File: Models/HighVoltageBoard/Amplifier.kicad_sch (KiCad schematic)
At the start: 13 parts, among them J4 Conn_01x03_Socket, J8 Conn_Coaxial, Q1 Q_NJFET_DSG, Q5 Q_NJFET_DSG, U1 PA95

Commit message: Save progress
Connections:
- net -IN: now also NT1.1; no longer NT1.2
- net SENSEN: now also NT1.2; no longer NT1.1
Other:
- moved on the sheet: NT1, R1, R5

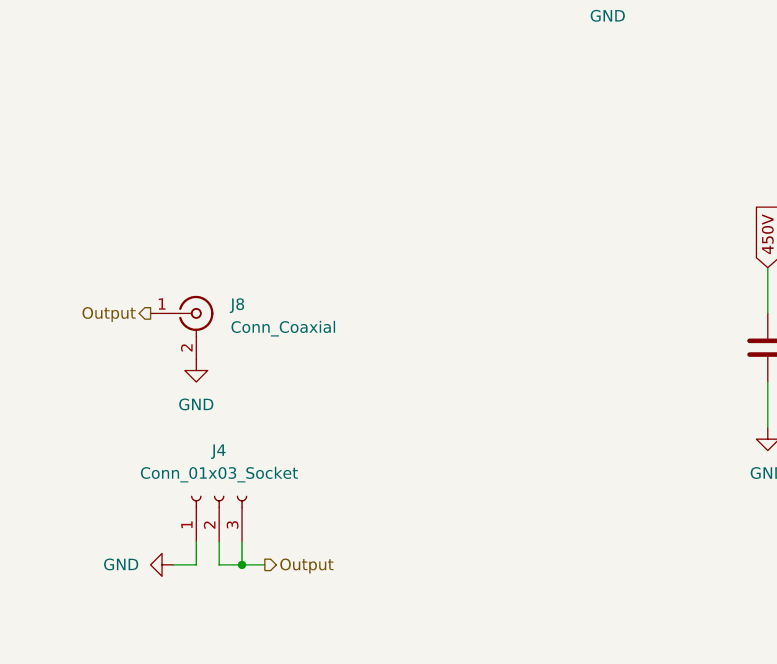
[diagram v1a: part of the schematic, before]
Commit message: Connectors should be fully specified now
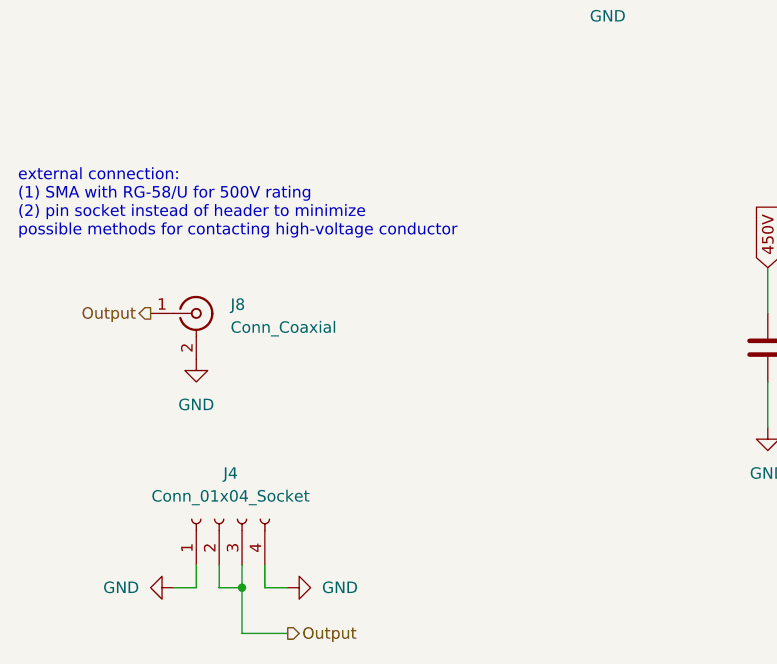
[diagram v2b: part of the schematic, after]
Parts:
- removed J4: Conn_01x03_Socket, symbol Connector:Conn_01x03_Socket
- added J4: Conn_01x04_Socket, symbol Connector:Conn_01x04_Socket
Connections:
- net GND: now also J4.1 (Pin_1), J4.4 (Pin_4)
- net Output: now also J4.2 (Pin_2), J4.3 (Pin_3)
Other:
- note added: "external connection: (1) SMA with RG-58/U for 500V rating (2) pin socket instead of header to minimize possible methods for contacting high-voltage conductor"

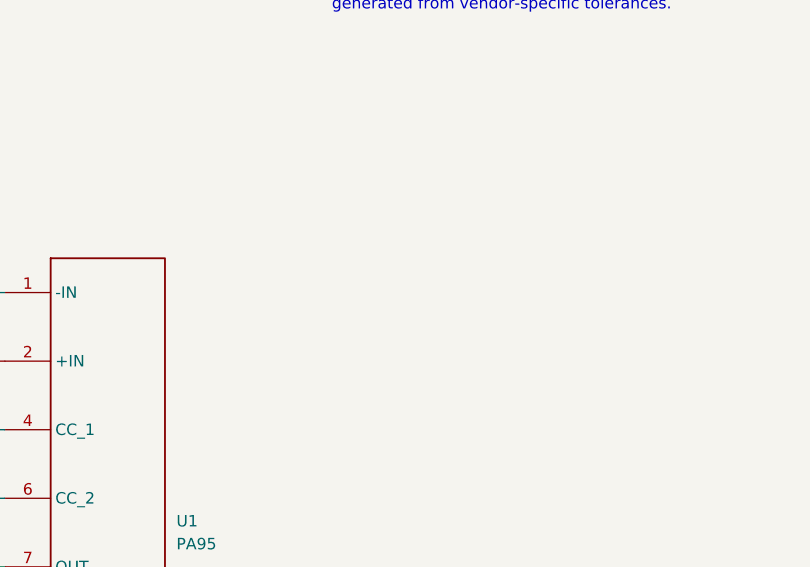
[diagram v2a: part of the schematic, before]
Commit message: Updated exclude from BOMs
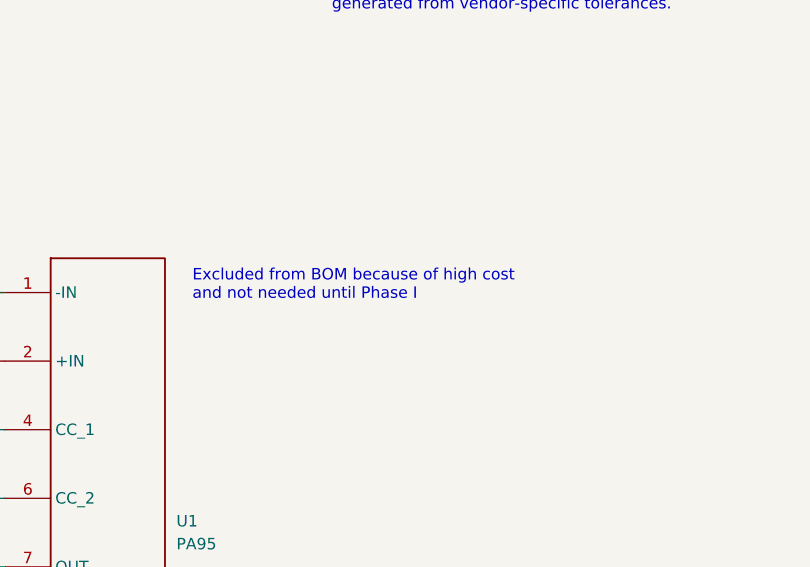
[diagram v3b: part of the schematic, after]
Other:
- note added: "Excluded from BOM because of high cost and not needed until Phase I"
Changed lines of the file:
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@@
+		)
+	)
+	(text "Excluded from BOM because of high cost\nand not needed until Phase I"
+		(exclude_from_sim no)
+		(at 218.948 66.04 0)
+		(effects
+			(font
+				(size 1.27 1.27)
+			)
+			(justify left top)
 		)
 	)

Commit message: Passes ERC
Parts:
- renumbered C5 to C1, C9 to C2, C1 to C3, J8 to J5, J4 to J6, NT5 to NT1, NT1 to NT2, Q5 to Q1, Q1 to Q2, R1 to R3, R5 to R4, R9 to R5

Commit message: Save progress
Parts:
- C1, C2: Cost (none) -> $0.646
- C3: Cost (none) -> $0.079
- Q1, Q2: Cost (none) -> $0.283
- R3: Cost (none) -> $0.089
- R4: Cost (none) -> $1.980
- R5: Cost (none) -> $0.041
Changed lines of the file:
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@@
+			)
+		)
+		(property "Cost" "$0.283"
+			(at 125.73 86.36 90)
+			(effects
+				(font
+					(size 1.27 1.27)
+				)
+				(hide yes)
 			)
 		)
@@
 			)
 		)
+		(property "Cost" "$0.041"
+			(at 177.8 102.87 0)
+			(effects
+				(font
+					(size 1.27 1.27)
+				)
+				(hide yes)
+			)
+		)
 		(pin "1"
 		)
@@
 			)
 		)
+		(property "Cost" "$0.283"
+			(at 97.79 82.55 90)
+			(effects
+				(font
+					(size 1.27 1.27)
+				)
+				(hide yes)
+			)
+		)
 		(pin "1"
 		)
@@
 			)
 		)
+		(property "Cost" "$0.646"
+			(at 114.3 143.51 0)
+			(effects
+				(font
+					(size 1.27 1.27)
+				)
+				(hide yes)
+			)
+		)
 		(pin "2"
 		)
@@
 			)
 		)
+		(property "Cost" "$0.079"
+			(at 182.88 87.63 0)
+			(effects
+				(font
+					(size 1.27 1.27)
+				)
+				(hide yes)
+			)
+		)
 		(pin "1"
 		)
@@
 		)
 		(property "Purchase Link" "https://www.digikey.com/en/products/detail/murata-electronics/GRJ55DR7LV474KW01L/16821217"
+			(at 139.7 143.51 0)
+			(effects
+				(font
+					(size 1.27 1.27)
+				)
+				(hide yes)
+			)
+		)
+		(property "Cost" "$0.646"
 			(at 139.7 143.51 0)
 			(effects
@@
 			)
 		)
+		(property "Cost" "$1.980"
+			(at 160.02 74.93 0)
+			(effects
+				(font
+					(size 1.27 1.27)
+				)
+				(hide yes)
+			)
+		)
 		(pin "2"
 		)
@@
 			(at 160.02 62.23 0)
 			(effects
+				(font
+					(size 1.27 1.27)
+				)
+				(hide yes)
+			)
+		)
+		(property "Cost" "$0.089"
+			(at 160.02 62.23 0)
+			(effects

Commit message: Should be finished with components BOM
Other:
- note removed: "Footprints for the large components: RESC1206 RESC1210 CAPC1206_CHV CAPC2220 To designate that they deviate from the standard Vishay resistor or Murata capacitor, a suffix is applied to a one-off footprint generated from vendor-specific tolerances."
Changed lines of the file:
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@@
-		)
-	)
-	(text "Footprints for the large components:\nRESC1206\nRESC1210\nCAPC1206_CHV\nCAPC2220\n\nTo designate that they deviate from the\nstandard Vishay resistor or Murata capacitor,\na suffix is applied to a one-off footprint\ngenerated from vendor-specific tolerances.\n"
-		(exclude_from_sim no)
-		(at 234.442 17.526 0)
-		(effects
-			(font
-				(size 1.27 1.27)
-			)
-			(justify left top)
 		)
 	)

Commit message: Save progress
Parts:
- U1: Cost (none) -> $283.630
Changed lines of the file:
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@@
+			)
+		)
+		(property "Cost" "$283.630"
+			(at 209.55 95.25 0)
+			(effects
+				(font
+					(size 1.27 1.27)
+				)
+				(hide yes)
 			)
 		)

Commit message: Assigned footprints
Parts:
- C1, C2: footprint (none) -> TwoTerminal:CAPC2220_GRJ
- C3: footprint (none) -> TwoTerminal:CAPC1206_CHV
- J5: footprint (none) -> Connector_Custom:RFPC-SMA27-F
- J6: footprint (none) -> Connector_Custom:PinConnector_1x4
- NT1, NT2: footprint (none) -> Connector_Custom:NetTie_0.2mm
- Q1, Q2: footprint (none) -> ThreeTerminal:SOT-23
- R4: footprint (none) -> TwoTerminal:RESC1210_TNPV
- R5: footprint (none) -> TwoTerminal:RESC0805
- U1: footprint (none) -> IC:PA95
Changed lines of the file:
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@@
 			)
 		)
-		(property "Footprint" ""
+		(property "Footprint" "Connector_Custom:NetTie_0.2mm"
 			(at 177.8 62.23 0)
 			(effects
@@
 			)
 		)
-		(property "Footprint" ""
+		(property "Footprint" "ThreeTerminal:SOT-23"
 			(at 123.19 81.28 0)
 			(effects
@@
 			)
 		)
-		(property "Footprint" ""
+		(property "Footprint" "Connector_Custom:RFPC-SMA27-F"
 			(at 50.8 139.7 0)
 			(effects
@@
 			)
 		)
-		(property "Footprint" ""
+		(property "Footprint" "IC:PA95"
 			(at 228.6 190.17 0)
 			(effects
@@
 			)
 		)
-		(property "Footprint" ""
+		(property "Footprint" "Connector_Custom:NetTie_0.2mm"
 			(at 170.18 99.06 0)
 			(effects
@@
 			)
 		)
-		(property "Footprint" ""
+		(property "Footprint" "TwoTerminal:RESC0805"
 			(at 176.784 102.616 90)
 			(effects
@@
 			)
 		)
-		(property "Footprint" ""
+		(property "Footprint" "ThreeTerminal:SOT-23"
 			(at 100.33 87.63 0)
 			(effects
@@
 			)
 		)
-		(property "Footprint" ""
+		(property "Footprint" "TwoTerminal:CAPC2220_GRJ"
 			(at 115.2652 147.32 0)
 			(effects
@@
 			)
 		)
-		(property "Footprint" ""
+		(property "Footprint" "TwoTerminal:CAPC1206_CHV"
 			(at 183.8452 91.44 0)
 			(effects
@@
 			)
 		)
-		(property "Footprint" ""
+		(property "Footprint" "Connector_Custom:PinConnector_1x4"
 			(at 53.34 162.56 0)
 			(effects
@@
 			)
 		)
-		(property "Footprint" ""
+		(property "Footprint" "TwoTerminal:CAPC2220_GRJ"
 			(at 140.6652 147.32 0)
 			(effects
@@
 			)
 		)
-		(property "Footprint" ""
+		(property "Footprint" "TwoTerminal:RESC1210_TNPV"
 			(at 161.036 75.184 90)
 			(effects
